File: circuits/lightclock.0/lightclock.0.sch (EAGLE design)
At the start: 0 parts

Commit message: 
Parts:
- added C1, C2, C3, C4: 0.1 uF, Kemper-Passives:CAP-0603
- added D1: LED-LRTDC9TP, Kemper-Passives:LED-LRTDC9TP
- added J1: USB-MINI-651005136421, Kemper-Connectors:USB-MINI-651005136421
- added L1: (no value), Kemper-Passives:IND-0603
- added R1: 11, Kemper-Passives:RES2010
- added R2: 6R2, Kemper-Passives:RES2010
- added R3: 6R8, Kemper-Passives:RES2010
- added U$1: RN-42, Kemper-DigitalIC:RN-42
- added U1: ATXMEGA-A4U, Kemper-DigitalIC:ATXMEGA-A4U
- added U2: DIODE-ESD-PRTR5V0U2X, Kemper-Passives:DIODE-ESD-PRTR5V0U2X
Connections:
- new net +3V3: C1.1, C2.1, C3.1, L1.P$1, U$1.VDD, U1.VCC0, U1.VCC1, U1.VDD
- new net +5V: R1.P$2, R2.P$2, R3.P$2
- new net BT_AUTO_DISC: U$1.PIO3
- new net BT_AUTO_MASTER: U$1.PIO6
- new net BT_CTS: U$1.UART_CTS
- new net BT_RESET: U$1.RESET
- new net BT_RTS: U$1.UART_RTS
- new net BT_RX: U$1.UART_RX
- new net BT_STATUS: U$1.PIO2
- new net BT_TX: U$1.UART_TX
- new net BT_TX/RX_STATUS: U$1.PIO8
- new net D+: J1.D+, U1.D+/PD7, U2.IO1
- new net D-: J1.D-, U1.D-/PD6, U2.IO2
- new net GND: C1.2, C2.2, C3.2, C4.2, J1.GND, U$1.GND0, U$1.GND1, U$1.GND2, U$1.GND3, U$1.PIO7, U1.GND0, U1.GND1, U1.GND2, U1.GND3, U2.GND
- new net N$1: C4.1, L1.P$2, U1.AVCC
- new net N$3: D1.A1, R1.P$1
- new net N$4: D1.A2, R2.P$1
- new net N$5: D1.A3, R3.P$1
- new net VBUS: J1.VBUS, U2.VCC

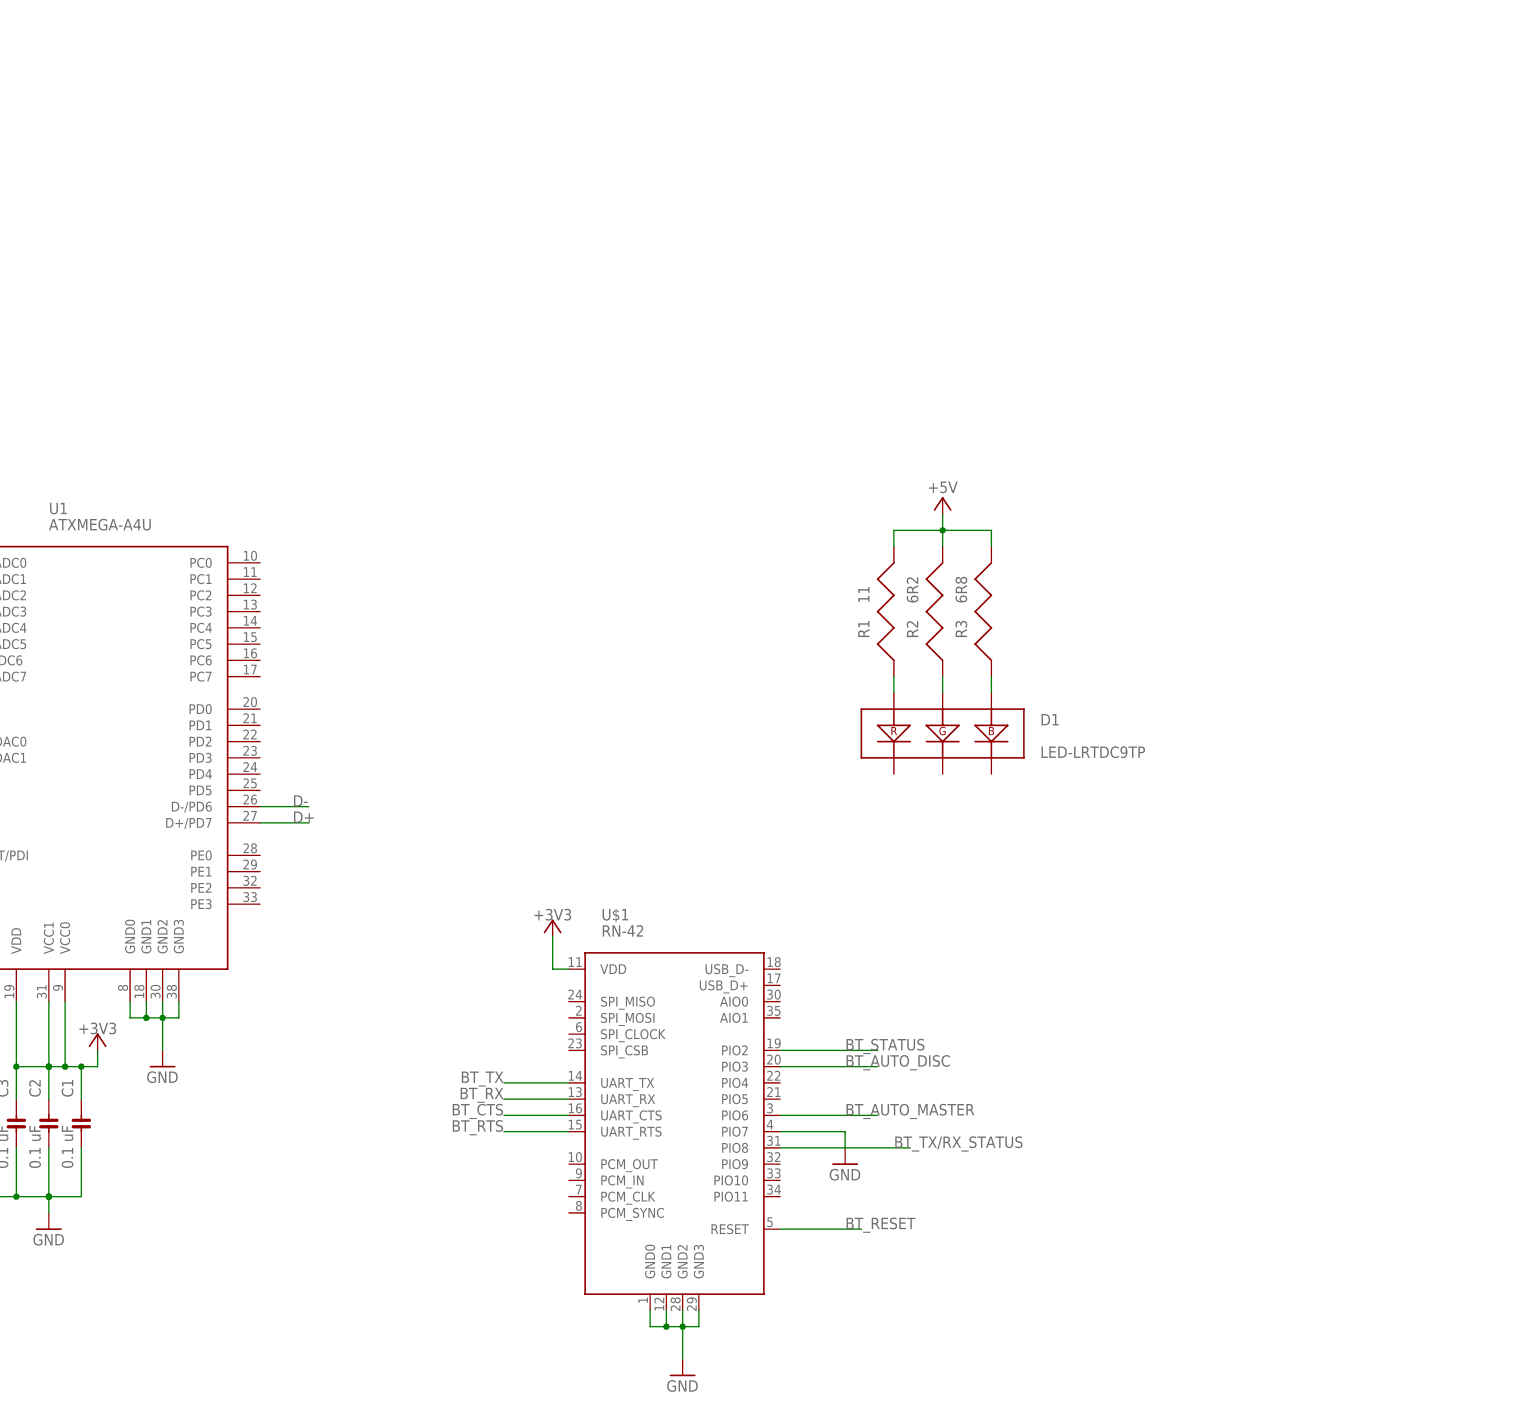
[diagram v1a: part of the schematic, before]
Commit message: 
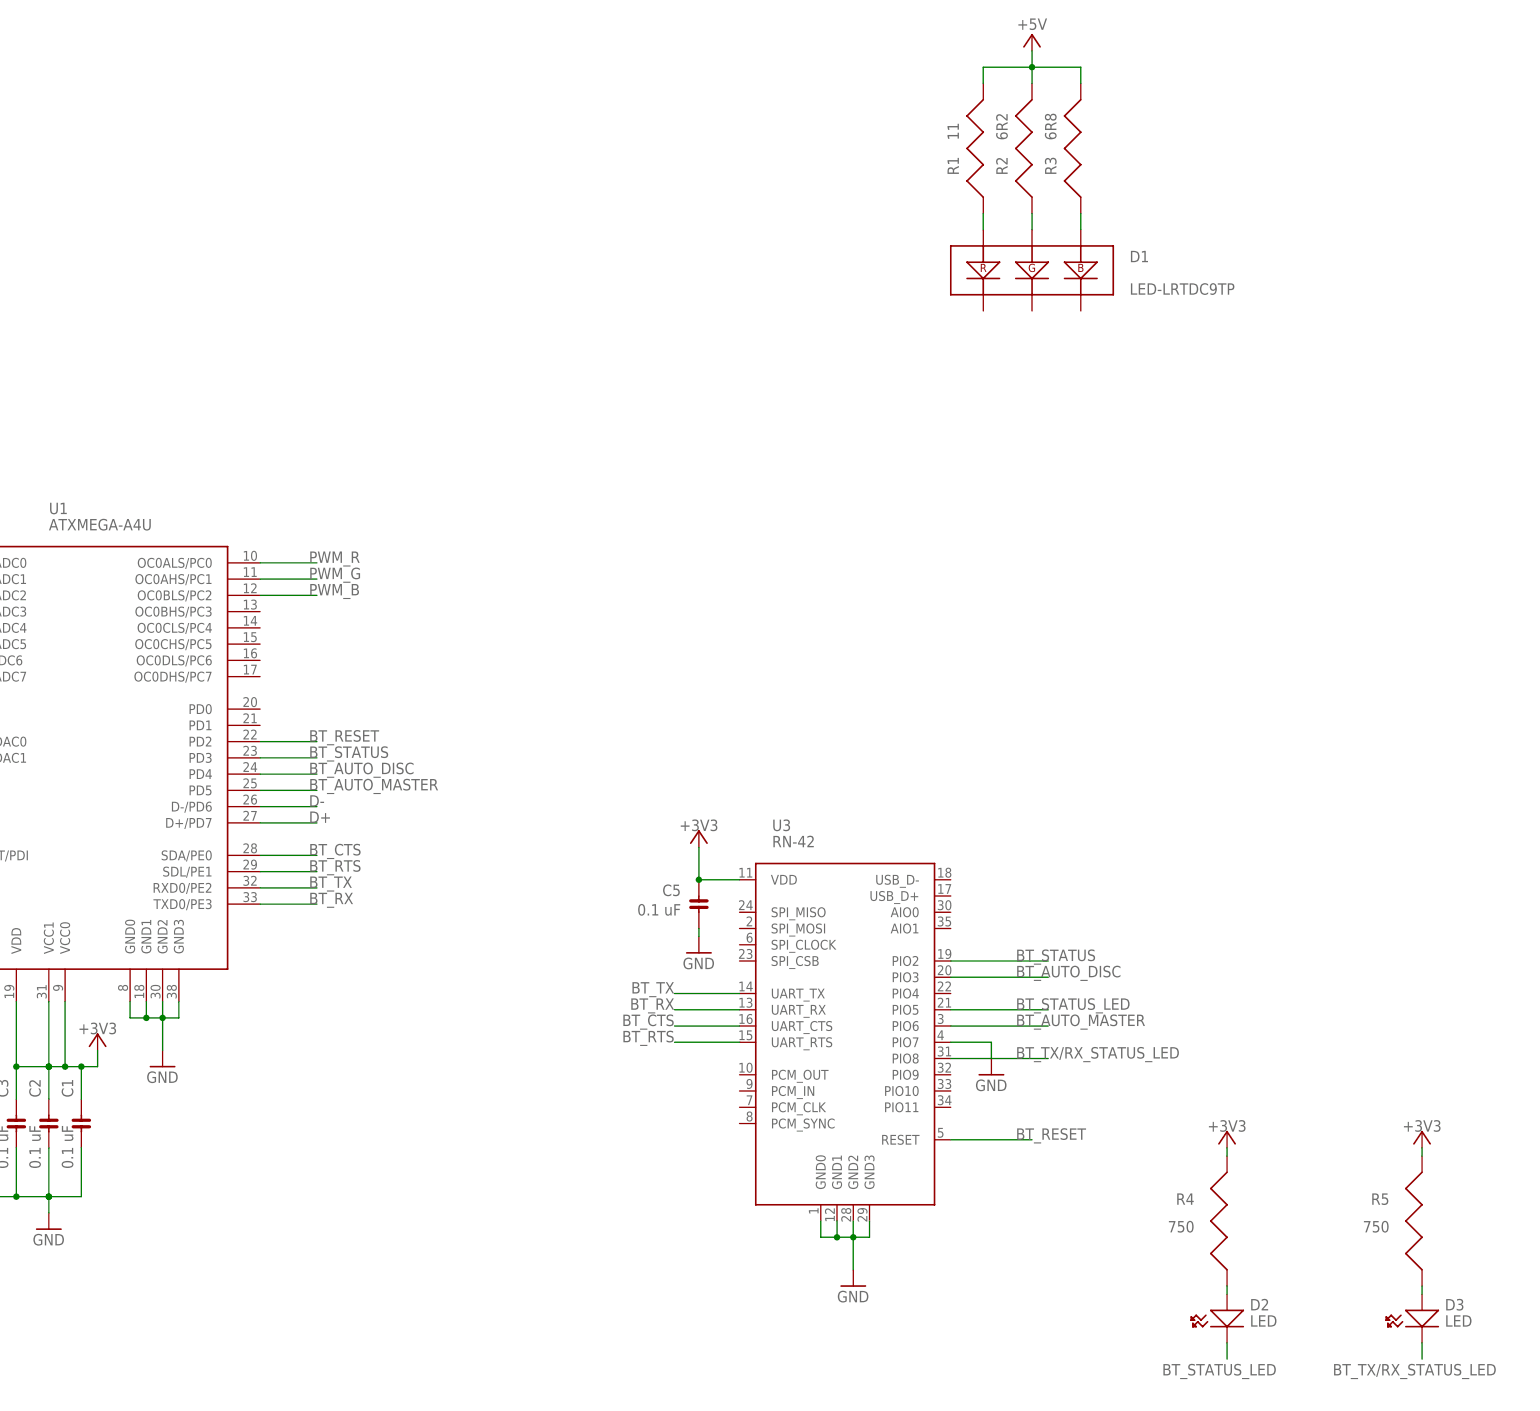
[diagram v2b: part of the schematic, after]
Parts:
- removed U$1: RN-42, Kemper-DigitalIC:RN-42
- added C5: 0.1 uF, Kemper-Passives:CAP-0603
- added D2, D3: LED, Kemper-Passives:LED
- added R4, R5: 750, Kemper-Passives:RES2010
- added U3: RN-42, Kemper-DigitalIC:RN-42
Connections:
- removed net BT_TX/RX_STATUS: U$1.PIO8
- new net BT_STATUS_LED: D2.2, U3.PIO5
- new net BT_TX/RX_STATUS_LED: D3.2, U3.PIO8
- new net N$2: D2.1, R4.P$1
- new net N$6: D3.1, R5.P$1
- new net PWM_B: U1.OC0BLS/PC2
- new net PWM_G: U1.OC0AHS/PC1
- new net PWM_R: U1.OC0ALS/PC0
- net +3V3: now also C5.1, R4.P$2, R5.P$2, U3.VDD; no longer U$1.VDD
- net BT_AUTO_DISC: now also U1.PD4, U3.PIO3; no longer U$1.PIO3
- net BT_AUTO_MASTER: now also U1.PD5, U3.PIO6; no longer U$1.PIO6
- net BT_CTS: now also U1.SDA/PE0, U3.UART_CTS; no longer U$1.UART_CTS
- net BT_RESET: now also U1.PD2, U3.RESET; no longer U$1.RESET
- net BT_RTS: now also U1.SDL/PE1, U3.UART_RTS; no longer U$1.UART_RTS
- net BT_RX: now also U1.TXD0/PE3, U3.UART_RX; no longer U$1.UART_RX
- net BT_STATUS: now also U1.PD3, U3.PIO2; no longer U$1.PIO2
- net BT_TX: now also U1.RXD0/PE2, U3.UART_TX; no longer U$1.UART_TX
- net GND: now also C5.2, U3.GND0, U3.GND1, U3.GND2, U3.GND3, U3.PIO7; no longer U$1.GND0, U$1.GND1, U$1.GND2, U$1.GND3, U$1.PIO7
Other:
- moved on the sheet: D1, R1, R2, R3

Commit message: 
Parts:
- added C6, C7: 1 uF, Kemper-Passives:CAP-0603
- added Q1, Q2, Q3: BSS138, Kemper-Passives:BSS138
- added U4: AP7313-33SAG-7, Kemper-DigitalIC:AP7313-33SAG-7
- R1: value 11 -> 18
- R2: value 6R2 -> 9R1
- R3: value 6R8 -> 13
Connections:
- new net N$12: C7.1, U4.OUT
- new net N$7: D1.C1, Q1.D
- new net N$8: D1.C2, Q2.D
- new net N$9: D1.C3, Q3.D
- net GND: now also C6.2, C7.2, Q1.S, Q2.S, Q3.S, U4.GND
- net PWM_B: now also Q3.G
- net PWM_G: now also Q2.G
- net PWM_R: now also Q1.G
- net VBUS: now also C6.1, U4.IN
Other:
- note added: "Kevin Kemper"
- moved on the sheet: D1, R1, R2, R3

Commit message: 
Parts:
- added C8: 10 uF, Kemper-Passives:CAP-0805
- added D4: LED, Kemper-Passives:LED
- added J10, J11, J12, J13, J14, J15, J16, J17, J2, J3, J4, J5, J6, J7, J8: TESTPAD, Kemper-Connectors:TESTPAD
- added J9: HEADER-2X6, Kemper-Connectors:HEADER-2X6
- added R7: 750, Kemper-Passives:RES-0603
- added S1: KMR211GLFS, Kemper-ElectroMechanical:KMR211GLFS
- R4, R5: device Kemper-Passives:RES2010 -> Kemper-Passives:RES-0603
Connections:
- new net N$10: D4.1, R7.P$1
- new net N$11: J7.P$1, U1.PD0
- new net N$13: J8.P$1, U1.PD1
- new net N$14: J6.P$1, U1.OC0DHS/PC7
- new net N$15: J5.P$1, U1.OC0DLS/PC6
- new net N$16: J4.P$1, U1.OC0CHS/PC5
- new net N$17: J3.P$1, U1.OC0CLS/PC4
- new net N$18: J2.P$1, U1.OC0BHS/PC3
- new net N$20: J10.P$1, U1.PA0/ADC0
- new net N$21: J11.P$1, U1.PA1/ADC1
- new net N$22: J12.P$1, U1.PA2/ADC2
- new net N$23: J13.P$1, U1.PA3/ADC3
- new net N$24: J14.P$1, U1.PA4/ADC4
- new net N$25: J15.P$1, U1.PA5/ADC5
- new net N$26: J16.P$1, U1.PA6ADC6
- new net N$27: J17.P$1, U1.PA7/ADC7
- new net PDI_CLK: J9.5, U1.!RESE!T/PDI_CLK
- new net PDI_DATA: J9.1, U1.PDI_DATA
- new net SWITCH: S1.3, S1.4, U1.PB0
- net +3V3: now also J9.2
- net GND: now also C8.2, D4.2, J9.6, S1.1, S1.2
- net N$12: now also R7.P$2
- net VBUS: now also C8.1
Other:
- note added: "USB Connector"
- moved on the sheet: C6, C7, D2, D3, J1, R4, R5, U2, U4

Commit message: 
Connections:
- removed net N$12: C7.1, R7.P$2, U4.OUT
- removed net VBUS: C6.1, C8.1, J1.VBUS, U2.VCC, U4.IN
- net +3V3: now also C7.1, R7.P$2, U4.OUT
- net +5V: now also C6.1, C8.1, J1.VBUS, U2.VCC, U4.IN
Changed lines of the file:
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@@
 <setting verticaltext="up"/>
 </settings>
-<grid distance="0.1" unitdist="inch" unit="inch" style="lines" multiple="1" display="yes" altdistance="0.01" altunitdist="inch" altunit="inch"/>
+<grid distance="0.1" unitdist="inch" unit="inch" style="lines" multiple="1" display="no" altdistance="0.01" altunitdist="inch" altunit="inch"/>
 <layers>
 <layer number="1" name="Top" color="4" fill="1" visible="no" active="no"/>
@@
 </segment>
 </net>
-<net name="VBUS" class="0">
-<segment>
-<pinref part="J1" gate="G$1" pin="VBUS"/>
-<wire x1="40.64" y1="248.92" x2="78.74" y2="248.92" width="0.1524" layer="91"/>
-<pinref part="U2" gate="G$1" pin="VCC"/>
-<wire x1="76.2" y1="233.68" x2="78.74" y2="233.68" width="0.1524" layer="91"/>
-<wire x1="78.74" y1="233.68" x2="78.74" y2="248.92" width="0.1524" layer="91"/>
-<wire x1="78.74" y1="248.92" x2="83.82" y2="248.92" width="0.1524" layer="91"/>
-<junction x="78.74" y="248.92"/>
-<label x="81.28" y="248.92" size="1.778" layer="95"/>
-<label x="81.28" y="248.92" size="1.778" layer="95"/>
-</segment>
-<segment>
-<pinref part="C6" gate="G$1" pin="1"/>
-<wire x1="162.56" y1="256.54" x2="162.56" y2="259.08" width="0.1524" layer="91"/>
-<pinref part="U4" gate="G$1" pin="IN"/>
-<wire x1="162.56" y1="259.08" x2="172.72" y2="259.08" width="0.1524" layer="91"/>
-<wire x1="162.56" y1="259.08" x2="147.32" y2="259.08" width="0.1524" layer="91"/>
-<junction x="162.56" y="259.08"/>
-<label x="139.7" y="259.08" size="1.778" layer="95" rot="MR0"/>
-<wire x1="147.32" y1="259.08" x2="142.24" y2="259.08" width="0.1524" layer="91"/>
-<wire x1="147.32" y1="256.54" x2="147.32" y2="259.08" width="0.1524" layer="91"/>
-<junction x="147.32" y="259.08"/>
-<pinref part="C8" gate="G$1" pin="1"/>
-</segment>
-</net>
 <net name="GND" class="0">
 <segment>
@@
 <wire x1="403.86" y1="78.74" x2="403.86" y2="81.28" width="0.1524" layer="91"/>
 </segment>
+<segment>
+<pinref part="U4" gate="G$1" pin="OUT"/>
+<pinref part="C7" gate="G$1" pin="1"/>
+<wire x1="193.04" y1="259.08" x2="203.2" y2="259.08" width="0.1524" layer="91"/>
+<wire x1="203.2" y1="259.08" x2="203.2" y2="256.54" width="0.1524" layer="91"/>
+<wire x1="203.2" y1="259.08" x2="220.98" y2="259.08" width="0.1524" layer="91"/>
+<junction x="203.2" y="259.08"/>
+<pinref part="+3V6" gate="G$1" pin="+3V3"/>
+<wire x1="220.98" y1="259.08" x2="231.14" y2="259.08" width="0.1524" layer="91"/>
+<wire x1="220.98" y1="256.54" x2="220.98" y2="259.08" width="0.1524" layer="91"/>
+<junction x="220.98" y="259.08"/>
+<pinref part="R7" gate="G$1" pin="P$2"/>
+</segment>
 </net>
 <net name="N$1" class="0">
@@
 <pinref part="R3" gate="G$1" pin="P$2"/>
 </segment>
+<segment>
+<pinref part="C6" gate="G$1" pin="1"/>
+<wire x1="162.56" y1="256.54" x2="162.56" y2="259.08" width="0.1524" layer="91"/>
+<pinref part="U4" gate="G$1" pin="IN"/>
+<wire x1="162.56" y1="259.08" x2="172.72" y2="259.08" width="0.1524" layer="91"/>
+<wire x1="162.56" y1="259.08" x2="147.32" y2="259.08" width="0.1524" layer="91"/>
+<junction x="162.56" y="259.08"/>
+<wire x1="147.32" y1="259.08" x2="142.24" y2="259.08" width="0.1524" layer="91"/>
+<wire x1="147.32" y1="256.54" x2="147.32" y2="259.08" width="0.1524" layer="91"/>
+<junction x="147.32" y="259.08"/>
+<pinref part="C8" gate="G$1" pin="1"/>
+<label x="137.16" y="259.08" size="1.778" layer="95"/>
+</segment>
+<segment>
+<pinref part="J1" gate="G$1" pin="VBUS"/>
+<wire x1="40.64" y1="248.92" x2="78.74" y2="248.92" width="0.1524" layer="91"/>
+<pinref part="U2" gate="G$1" pin="VCC"/>
+<wire x1="76.2" y1="233.68" x2="78.74" y2="233.68" width="0.1524" layer="91"/>
+<wire x1="78.74" y1="233.68" x2="78.74" y2="248.92" width="0.1524" layer="91"/>
+<wire x1="78.74" y1="248.92" x2="83.82" y2="248.92" width="0.1524" layer="91"/>
+<junction x="78.74" y="248.92"/>
+<label x="81.28" y="248.92" size="1.778" layer="95"/>
+<label x="81.28" y="248.92" size="1.778" layer="95"/>
+</segment>
 </net>
 <net name="N$3" class="0">
@@
 <pinref part="Q3" gate="G$1" pin="D"/>
 <wire x1="347.98" y1="208.28" x2="347.98" y2="185.42" width="0.1524" layer="91"/>
-</segment>
-</net>
-<net name="N$12" class="0">
-<segment>
-<pinref part="U4" gate="G$1" pin="OUT"/>
-<pinref part="C7" gate="G$1" pin="1"/>
-<wire x1="193.04" y1="259.08" x2="203.2" y2="259.08" width="0.1524" layer="91"/>
-<wire x1="203.2" y1="259.08" x2="203.2" y2="256.54" width="0.1524" layer="91"/>
-<wire x1="203.2" y1="259.08" x2="220.98" y2="259.08" width="0.1524" layer="91"/>
-<junction x="203.2" y="259.08"/>
-<pinref part="+3V6" gate="G$1" pin="+3V3"/>
-<wire x1="220.98" y1="259.08" x2="231.14" y2="259.08" width="0.1524" layer="91"/>
-<wire x1="220.98" y1="256.54" x2="220.98" y2="259.08" width="0.1524" layer="91"/>
-<junction x="220.98" y="259.08"/>
-<pinref part="R7" gate="G$1" pin="P$2"/>
 </segment>
 </net>
@@
 </segment>
 </net>
-<net name="N$19" class="0">
-<segment>
-<wire x1="22.86" y1="264.16" x2="91.44" y2="264.16" width="0.2032" layer="91" style="longdash"/>
-<wire x1="91.44" y1="264.16" x2="91.44" y2="208.28" width="0.2032" layer="91" style="longdash"/>
-<wire x1="91.44" y1="208.28" x2="22.86" y2="208.28" width="0.2032" layer="91" style="longdash"/>
-<wire x1="22.86" y1="208.28" x2="22.86" y2="264.16" width="0.2032" layer="91" style="longdash"/>
-</segment>
-</net>

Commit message: almost done with layout, just needs a review
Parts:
- added J18, J19, J20, J21: TESTPAD, Kemper-Connectors:TESTPAD
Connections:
- net +3V3: now also J18.P$1, J20.P$1
- net GND: now also J19.P$1, J21.P$1
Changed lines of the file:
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@@
 <setting verticaltext="up"/>
 </settings>
-<grid distance="0.1" unitdist="inch" unit="inch" style="lines" multiple="1" display="no" altdistance="0.01" altunitdist="inch" altunit="inch"/>
+<grid distance="0.1" unitdist="inch" unit="inch" style="lines" multiple="1" display="yes" altdistance="0.01" altunitdist="inch" altunit="inch"/>
 <layers>
 <layer number="1" name="Top" color="4" fill="1" visible="no" active="no"/>
@@
 <part name="R5" library="Kemper-Passives" deviceset="RES-0603" device="" value="750"/>
 <part name="R7" library="Kemper-Passives" deviceset="RES-0603" device="" value="750"/>
+<part name="J18" library="Kemper-Connectors" deviceset="TESTPAD" device=""/>
+<part name="J19" library="Kemper-Connectors" deviceset="TESTPAD" device=""/>
+<part name="J20" library="Kemper-Connectors" deviceset="TESTPAD" device=""/>
+<part name="J21" library="Kemper-Connectors" deviceset="TESTPAD" device=""/>
+<part name="GND16" library="supply1" deviceset="GND" device=""/>
+<part name="GND17" library="supply1" deviceset="GND" device=""/>
+<part name="+3V8" library="supply1" deviceset="+3V3" device=""/>
+<part name="+3V9" library="supply1" deviceset="+3V3" device=""/>
 </parts>
 <sheets>
@@
 <attribute name="NAME" x="223.52" y="248.92" size="1.778" layer="95"/>
 <attribute name="VALUE" x="223.52" y="246.38" size="1.778" layer="96" rot="MR180"/>
+</instance>
+<instance part="J18" gate="G$1" x="154.94" y="182.88" rot="R180"/>
+<instance part="J19" gate="G$1" x="154.94" y="180.34" rot="R180"/>
+<instance part="J20" gate="G$1" x="233.68" y="187.96"/>
+<instance part="J21" gate="G$1" x="233.68" y="185.42"/>
+<instance part="GND16" gate="1" x="228.6" y="182.88"/>
+<instance part="GND17" gate="1" x="160.02" y="177.8"/>
+<instance part="+3V8" gate="G$1" x="228.6" y="190.5" smashed="yes" rot="MR0">
+<attribute name="VALUE" x="228.6" y="190.5" size="1.778" layer="96" align="bottom-center"/>
+</instance>
+<instance part="+3V9" gate="G$1" x="160.02" y="185.42" smashed="yes" rot="MR0">
+<attribute name="VALUE" x="160.02" y="185.42" size="1.778" layer="96" align="bottom-center"/>
 </instance>
 </instances>
@@
 <wire x1="147.32" y1="248.92" x2="147.32" y2="246.38" width="0.1524" layer="91"/>
 <pinref part="C8" gate="G$1" pin="2"/>
+</segment>
+<segment>
+<pinref part="J19" gate="G$1" pin="P$1"/>
+<pinref part="GND17" gate="1" pin="GND"/>
+<wire x1="157.48" y1="180.34" x2="160.02" y2="180.34" width="0.1524" layer="91"/>
+</segment>
+<segment>
+<pinref part="GND16" gate="1" pin="GND"/>
+<pinref part="J21" gate="G$1" pin="P$1"/>
+<wire x1="228.6" y1="185.42" x2="231.14" y2="185.42" width="0.1524" layer="91"/>
 </segment>
 </net>
@@
 <pinref part="R7" gate="G$1" pin="P$2"/>
 </segment>
+<segment>
+<pinref part="J18" gate="G$1" pin="P$1"/>
+<pinref part="+3V9" gate="G$1" pin="+3V3"/>
+<wire x1="157.48" y1="182.88" x2="160.02" y2="182.88" width="0.1524" layer="91"/>
+</segment>
+<segment>
+<pinref part="J20" gate="G$1" pin="P$1"/>
+<pinref part="+3V8" gate="G$1" pin="+3V3"/>
+<wire x1="231.14" y1="187.96" x2="228.6" y2="187.96" width="0.1524" layer="91"/>
+</segment>
 </net>
 <net name="N$1" class="0">
@@
 </sheet>
 </sheets>
+<errors>
+</errors>
 </schematic>
 </drawing>
